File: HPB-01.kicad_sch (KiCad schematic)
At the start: 62 parts, among them J1 USB_A, J2 USB_B_Micro, J3 USB_A, J4 USB_C_Receptacle_USB2.0, J5 Pad, J6 Pad, J7 Battery Pad, J8 Battery Pad, Q1 RU207C, Q2 RU207C, Q3 RU20P7C, Q4 RU20P7C, Q5 IRF7832, Q6 IRF7832, SW1 SW_Push, U1 S-8261ABJMD-G3JT2S, U2 IP5328P

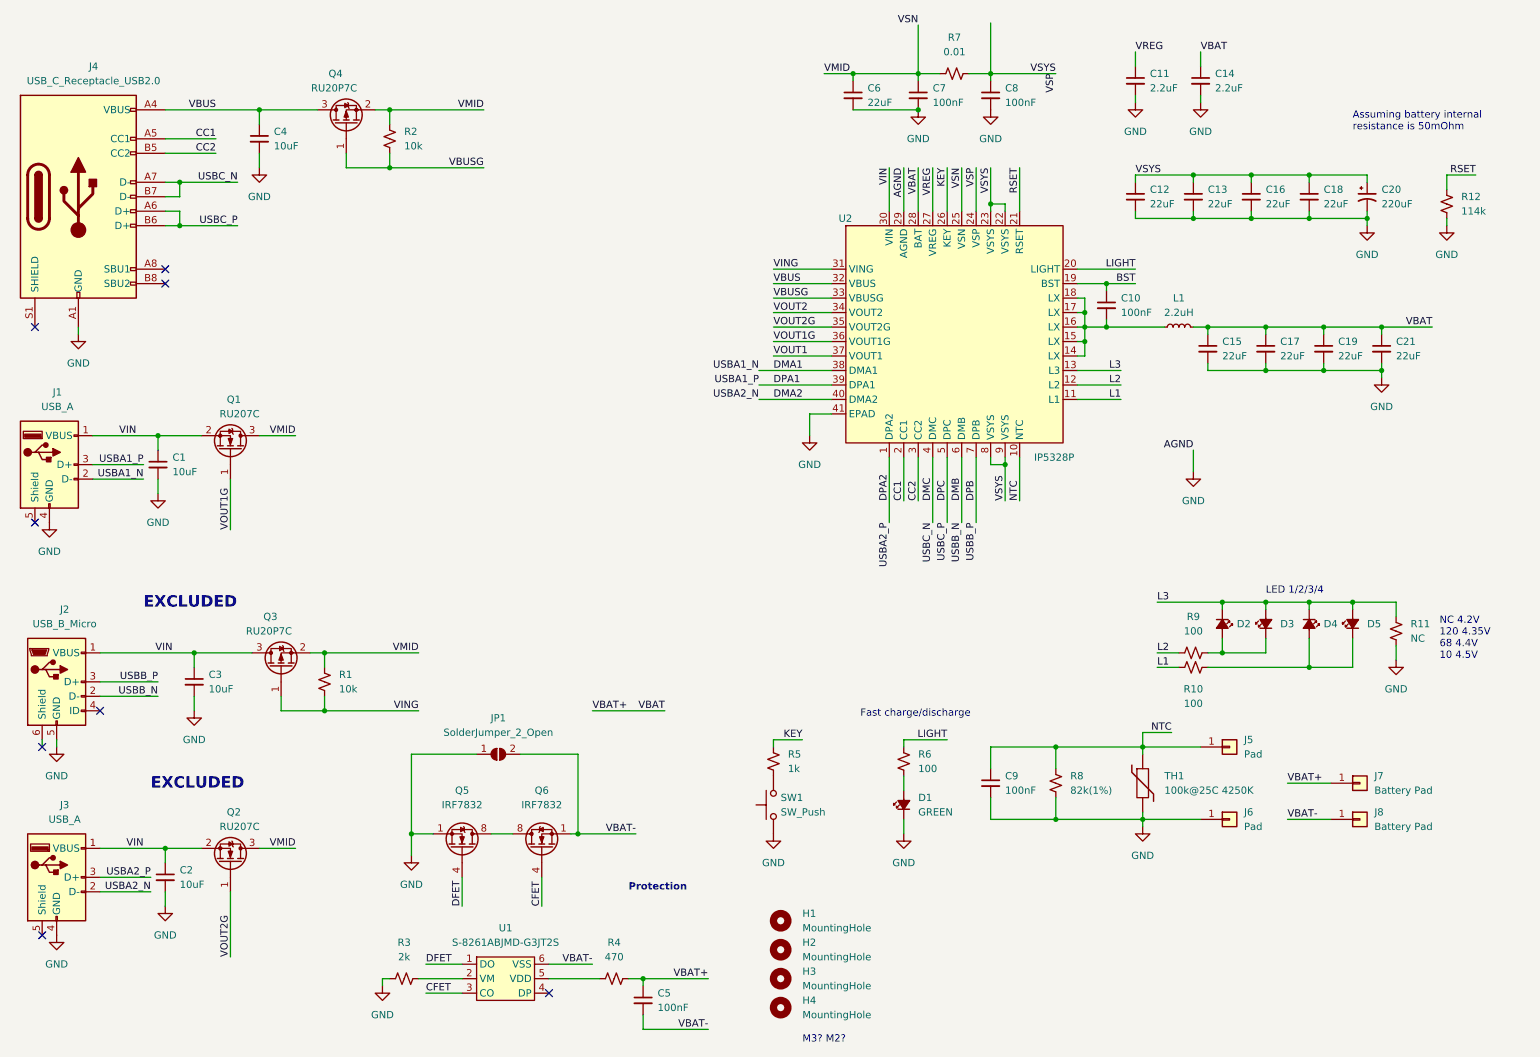
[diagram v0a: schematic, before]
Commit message: ERC and DRC correction
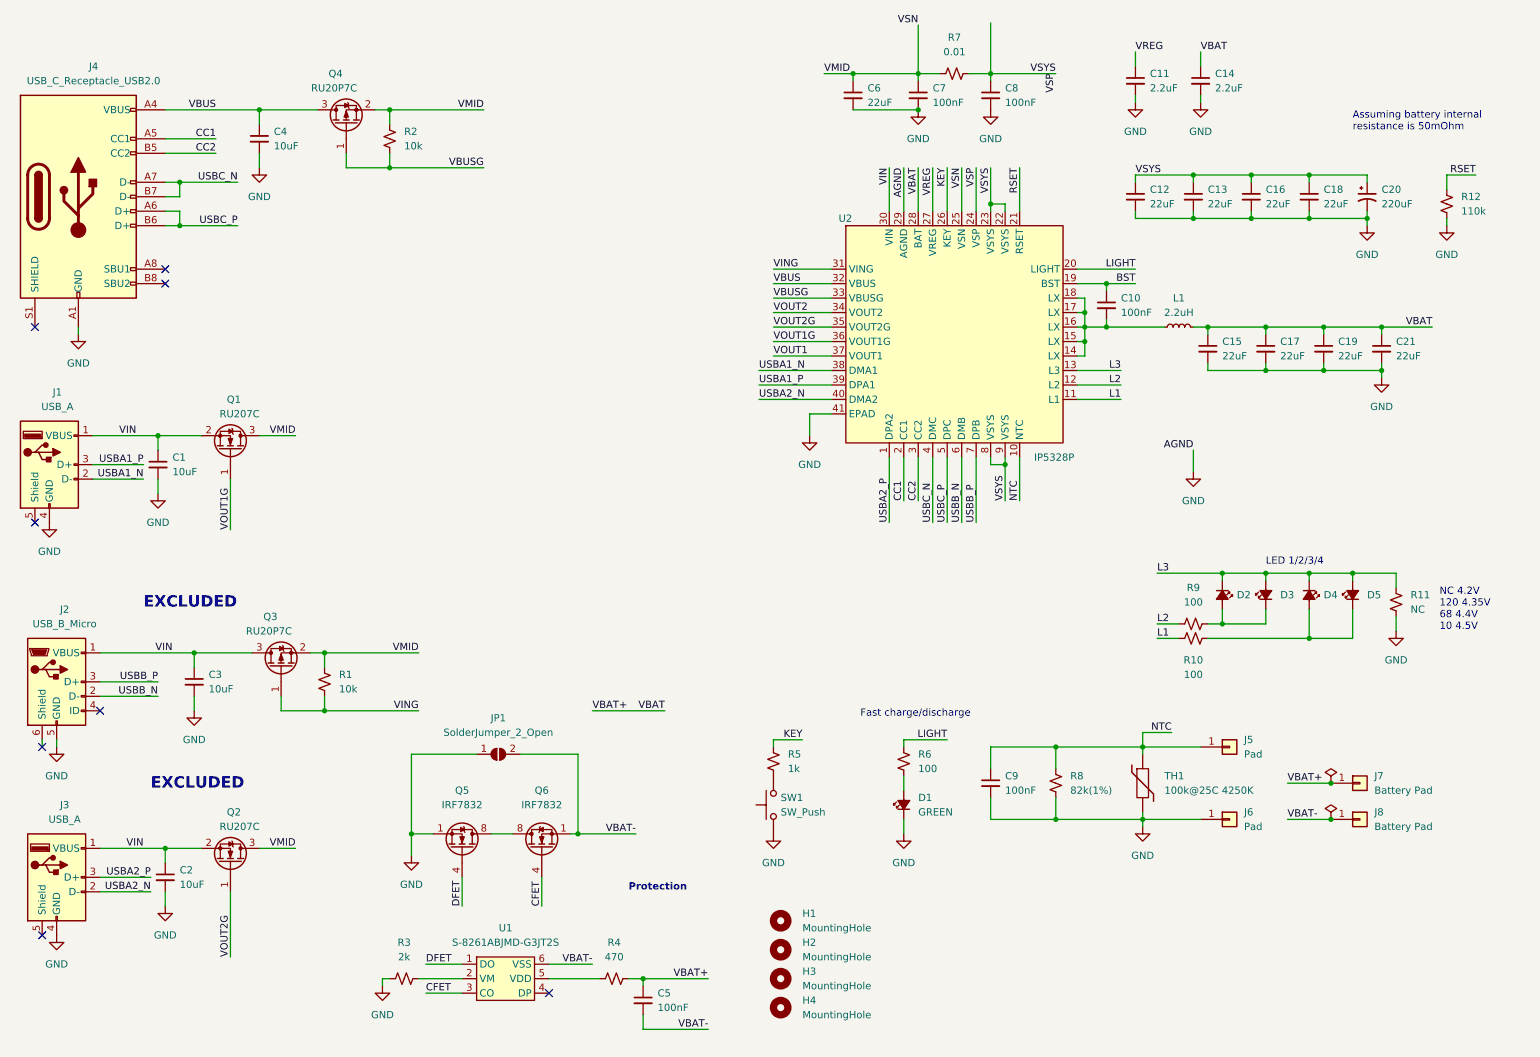
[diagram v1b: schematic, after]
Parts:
- R1, R2: LCSC (none) -> C25804
- R10, R6, R9: LCSC (none) -> C22775
- R12: value 114k -> 110k; LCSC (none) -> C25805
- R3: LCSC (none) -> C22975
- R4: LCSC (none) -> C23179
- R5: LCSC (none) -> C21190
- R7: LCSC (none) -> C309628
- R8: LCSC (none) -> C23254
- U2: LCSC (none) -> C188809
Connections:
- net DMA1 renamed USBA1_N
- net DMA2 renamed USBA2_N
- net DMB renamed USBB_N
- net DMC renamed USBC_N
- net DPA1 renamed USBA1_P
- net DPA2 renamed USBA2_P
- net DPB renamed USBB_P
- net DPC renamed USBC_P
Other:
- note removed: "M3? M2?"
- moved on the sheet: D2, D3, D4, D5, R10, R11, R9

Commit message: Change the layout (bigger)
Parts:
- removed C20: 220uF, Capacitor_SMD:CP_Elec_8x10.5, symbol Device:C_Polarized_Small_US
- added C20, C22, C23, C24: 22uF, Capacitor_SMD:C_0805_2012Metric, symbol Device:C_Small
- J7, J8: footprint TestPoint:TestPoint_Pad_4.0x4.0mm -> (none)
- SW1: footprint huconn-footprint:tact_switch 1TS002G-1300-3500-CT -> Button_Switch_SMD:SW_Push_1P1T-MP_NO_Horizontal_Alps_SKRTLAE010; LCSC C319392 -> C127481
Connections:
- net GND: now also C20.2, C22.2, C23.2, C24.2
- net VSP: now also C20.1, C22.1, C23.1, C24.1
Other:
- moved on the sheet: C12, C13, C16, C18

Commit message: [WIP] positioning parts on new layout (90%)
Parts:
- J1: footprint Connector_USB:USB_A_CONNFLY_DS1095-WNR0 -> HUCONN-Connector_USB:USB_A_FEMALE_905-662A203S10200; LCSC C2345 -> C41014
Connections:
- net VSP: no longer C12.1, C13.1, C16.1, C18.1, C20.1, C22.1, C23.1, C24.1, C8.1, R7.2, U2.22 (VSYS), U2.23 (VSYS), U2.24 (VSP), U2.8 (VSYS), U2.9 (VSYS)
- new net VSYS: C12.1, C13.1, C16.1, C18.1, C20.1, C22.1, C23.1, C24.1, C8.1, R7.2, U2.22 (VSYS), U2.23 (VSYS), U2.24 (VSP), U2.8 (VSYS), U2.9 (VSYS)
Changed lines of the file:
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@@
     (effects (font (size 1.27 1.27)) (justify right bottom))
   )
-  (label "VSP" (at 191.77 43.18 270)
+  (label "VSP" (at 208.28 38.1 270)
     (effects (font (size 1.27 1.27)) (justify right bottom))
   )
@@
     (effects (font (size 1.27 1.27)) (justify left bottom))
   )
-  (label "VSP" (at 205.74 26.67 270)
+  (label "VSP" (at 208.28 30.48 270)
     (effects (font (size 1.27 1.27)) (justify right bottom))
   )
@@
   (label "VBUS" (at 156.21 63.5 0)
     (effects (font (size 1.27 1.27)) (justify left bottom))
+  )
+  (label "VSYS" (at 191.77 43.18 270)
+    (effects (font (size 1.27 1.27)) (justify right bottom))
   )
   (label "USBC_N" (at 184.15 105.41 90)
@@
     (property "Reference" "J1" (id 0) (at 30.607 82.55 0))
     (property "Value" "USB_A" (id 1) (at 30.607 85.09 0))
-    (property "Footprint" "Connector_USB:USB_A_CONNFLY_DS1095-WNR0" (id 2) (at 33.02 96.52 0)
+    (property "Footprint" "HUCONN-Connector_USB:USB_A_FEMALE_905-662A203S10200" (id 2) (at 33.02 96.52 0)
       (effects (font (size 1.27 1.27)) hide)
     )
@@
       (effects (font (size 1.27 1.27)) hide)
     )
-    (property "LCSC" "C2345" (id 4) (at 29.21 95.25 0)
+    (property "LCSC" "C41014" (id 4) (at 29.21 95.25 0)
       (effects (font (size 1.27 1.27)) hide)
     )
@@
     )
     (path "/7175ab0c-615f-4b9c-bf15-51020ecf4cac"
-      (reference "J1") (unit 1) (value "USB_A") (footprint "Connector_USB:USB_A_CONNFLY_DS1095-WNR0")
+      (reference "J1") (unit 1) (value "USB_A") (footprint "HUCONN-Connector_USB:USB_A_FEMALE_905-662A203S10200")
     )
     (path "/19a81317-e9f1-4d34-9a71-b15696bab823"

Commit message: Add some comment for MP
Add 3D part archive
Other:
- note added: "25 50 75 100"
- note added: "TH1 is NC on MP"
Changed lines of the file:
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@@
     (effects (font (size 1.27 1.27) (thickness 0.254) bold) (justify left bottom))
+  )
+  (text "TH1 is NC on MP" (at 226.06 163.83 0)
+    (effects (font (size 1.27 1.27)) (justify left bottom))
   )
   (text "Fast charge/discharge" (at 171.45 139.7 0)
     (effects (font (size 1.27 1.27)) (justify left bottom))
   )
+  (text "25 50 75 100" (at 240.03 129.54 0)
+    (effects (font (size 1.27 1.27)) (justify left bottom))
+  )

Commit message: update library and 3d model
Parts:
- J1: footprint HUCONN-Connector_USB:USB_A_FEMALE_905-662A203S10200 -> Library:USB_A_FEMALE_905-662A203S10200
- SW1: footprint Button_Switch_SMD:SW_Push_1P1T-MP_NO_Horizontal_Alps_SKRTLAE010 -> Library:1TS003B-1900-4500A-CT_C349395; LCSC C127481 -> C349395
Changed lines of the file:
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@@
     (property "Reference" "J1" (id 0) (at 30.607 82.55 0))
     (property "Value" "USB_A" (id 1) (at 30.607 85.09 0))
-    (property "Footprint" "HUCONN-Connector_USB:USB_A_FEMALE_905-662A203S10200" (id 2) (at 33.02 96.52 0)
+    (property "Footprint" "Library:USB_A_FEMALE_905-662A203S10200" (id 2) (at 33.02 96.52 0)
       (effects (font (size 1.27 1.27)) hide)
     )
@@
       (effects (font (size 1.27 1.27)) (justify right))
     )
-    (property "Footprint" "Button_Switch_SMD:SW_Push_1P1T-MP_NO_Horizontal_Alps_SKRTLAE010" (id 2) (at 151.13 154.94 0)
+    (property "Footprint" "Library:1TS003B-1900-4500A-CT_C349395" (id 2) (at 151.13 154.94 0)
       (effects (font (size 1.27 1.27)) hide)
     )
@@
       (effects (font (size 1.27 1.27)) hide)
     )
-    (property "LCSC" "C127481" (id 4) (at 156.21 154.94 90)
+    (property "LCSC" "C349395" (id 4) (at 156.21 154.94 90)
       (effects (font (size 1.27 1.27)) hide)
     )
@@
     )
     (path "/7175ab0c-615f-4b9c-bf15-51020ecf4cac"
-      (reference "J1") (unit 1) (value "USB_A") (footprint "HUCONN-Connector_USB:USB_A_FEMALE_905-662A203S10200")
+      (reference "J1") (unit 1) (value "USB_A") (footprint "Library:USB_A_FEMALE_905-662A203S10200")
     )
     (path "/19a81317-e9f1-4d34-9a71-b15696bab823"
@@
     )
     (path "/bc43b947-844a-4301-b80a-09fe984eb0f5"
-      (reference "SW1") (unit 1) (value "SW_Push") (footprint "Button_Switch_SMD:SW_Push_1P1T-MP_NO_Horizontal_Alps_SKRTLAE010")
+      (reference "SW1") (unit 1) (value "SW_Push") (footprint "Library:1TS003B-1900-4500A-CT_C349395")
     )
     (path "/7434b9ec-7446-4163-8ac1-7817e9d6b81b"

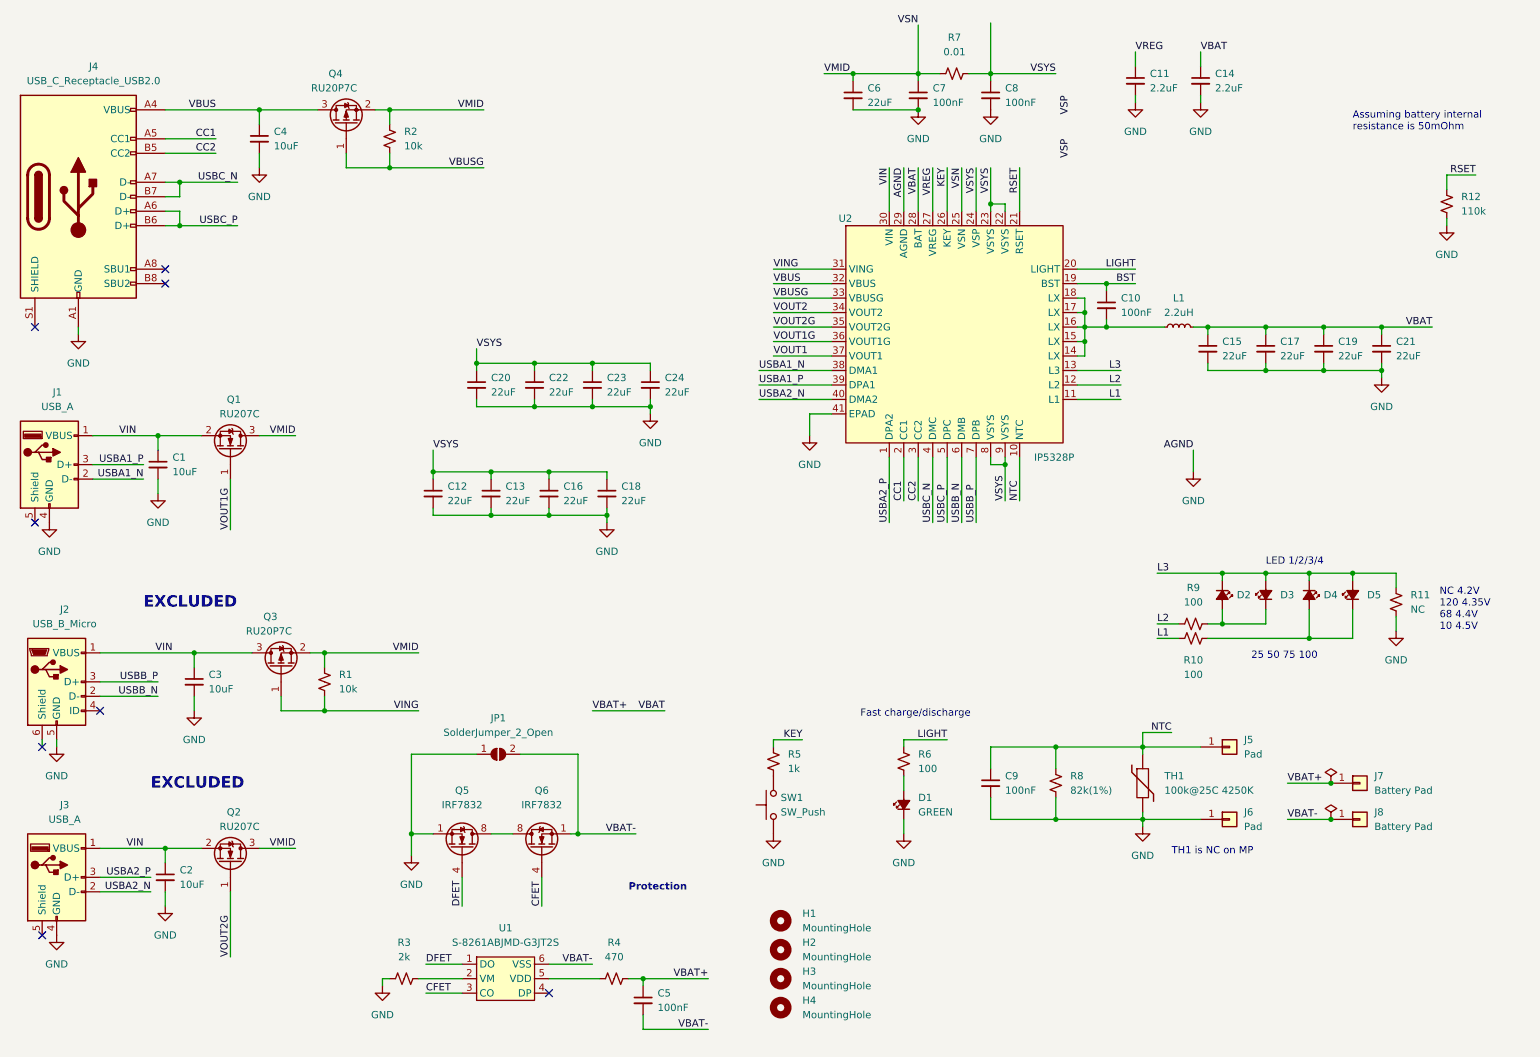
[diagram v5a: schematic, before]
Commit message: WIP: bug fix and make some improvement
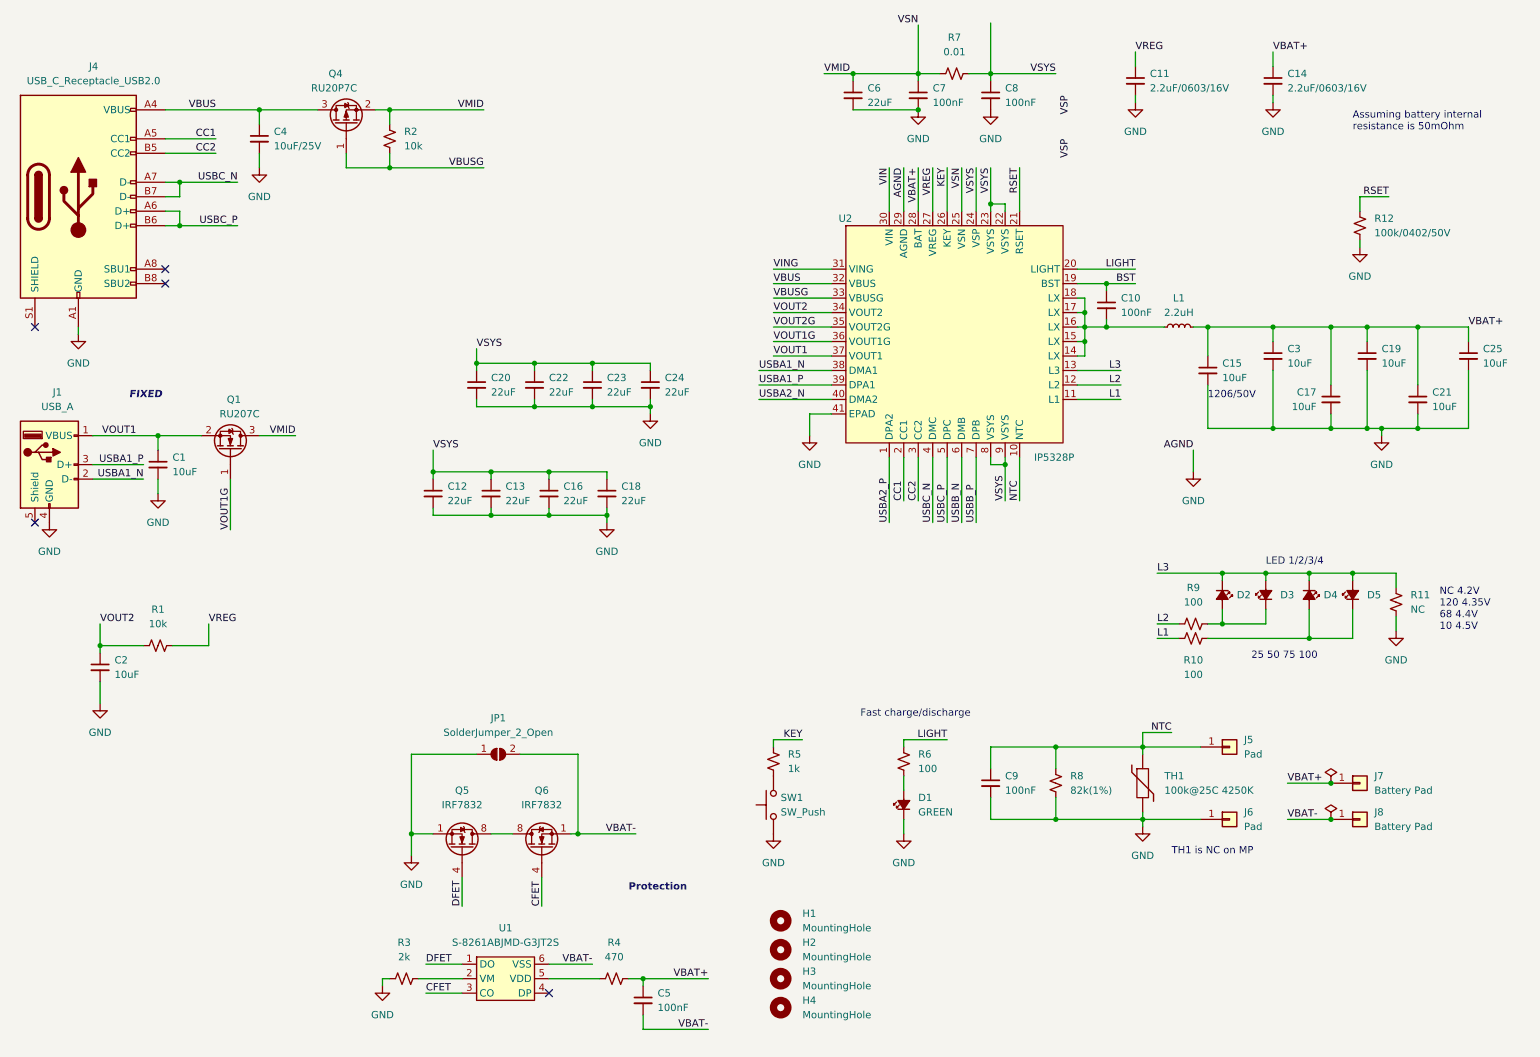
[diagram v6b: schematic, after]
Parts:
- removed J2: USB_B_Micro, Connector_USB:USB_Micro-B_Amphenol_10118194_Horizontal, symbol Connector:USB_B_Micro
- removed J3: USB_A, Connector_USB:USB_A_CONNFLY_DS1095-WNR0, symbol Connector:USB_A
- removed Q2: RU207C, Package_TO_SOT_SMD:SOT-23, symbol Transistor_FET:DMN3404L
- removed Q3: RU20P7C, Package_TO_SOT_SMD:SOT-23, symbol Transistor_FET:AO3401A
- added C25: 10uF, Capacitor_SMD:C_1206_3216Metric, symbol Device:C_Small
- C11, C14: value 2.2uF -> 2.2uF/0603/16V
- C15, C17, C19, C21: value 22uF -> 10uF; footprint Capacitor_SMD:C_0805_2012Metric -> Capacitor_SMD:C_1206_3216Metric; LCSC C45783 -> C13585
- C2, R1: now in the parts list
- C3: footprint Capacitor_SMD:C_0603_1608Metric -> Capacitor_SMD:C_1206_3216Metric; LCSC C96446 -> C13585; now in the parts list
- C4: value 10uF -> 10uF/25V
- J1: footprint Library:USB_A_FEMALE_905-662A203S10200 -> HUCONN-Connector_USB:USB_A_FEMALE_905-662A203S10200
- R12: value 110k -> 100k/0402/50V; footprint Resistor_SMD:R_0603_1608Metric -> Resistor_SMD:R_0402_1005Metric; LCSC C25805 -> C25086
- SW1: footprint Library:1TS003B-1900-4500A-CT_C349395 -> Button_Switch_SMD:SW_Push_1P1T-MP_NO_Horizontal_Alps_SKRTLAE010; LCSC C349395 -> C127481
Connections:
- net GND: now also C25.2
- net VIN: no longer C1.1, C2.1, C3.1, J1.1 (VBUS), Q1.2 (S)
- net VING: no longer R1.2
- net VMID: no longer R1.1
- net VOUT1: now also C1.1, J1.1 (VBUS), Q1.2 (S)
- net VOUT2: now also C2.1, R1.1
- net VREG: now also R1.2
- net VBAT renamed VBAT+
- net VBAT+: now also C3.1, C25.1
- no-connect marks 8 -> 5
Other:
- note added: "1206/50V"
- note added: "FIXED"
- note removed: "EXCLUDED"
- moved on the sheet: C14, C15, R12
